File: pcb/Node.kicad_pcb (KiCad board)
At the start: 4 copper layers, 50 x 50 mm, 138 parts, among them J1 LCD, J10 SPI, J13 Power, J14 SERIAL, J2 USB_C_USB2.0_16P, J3 INDICATOR, J4 GPB[0..3], J5 GPB[4..7], J7 GPA[4..7], J8 QWIIC1, J9 QWIIC2, Q1 MMBT2222A, SW1 RESET, SW2 BOOT, U1 ESP32-S3-WROOM-1-N8R2, U2 LM66200DRLR, U3 USBLC6-2P6, U4 MCP23017_ML, U5 LD1117S33TR_SOT223

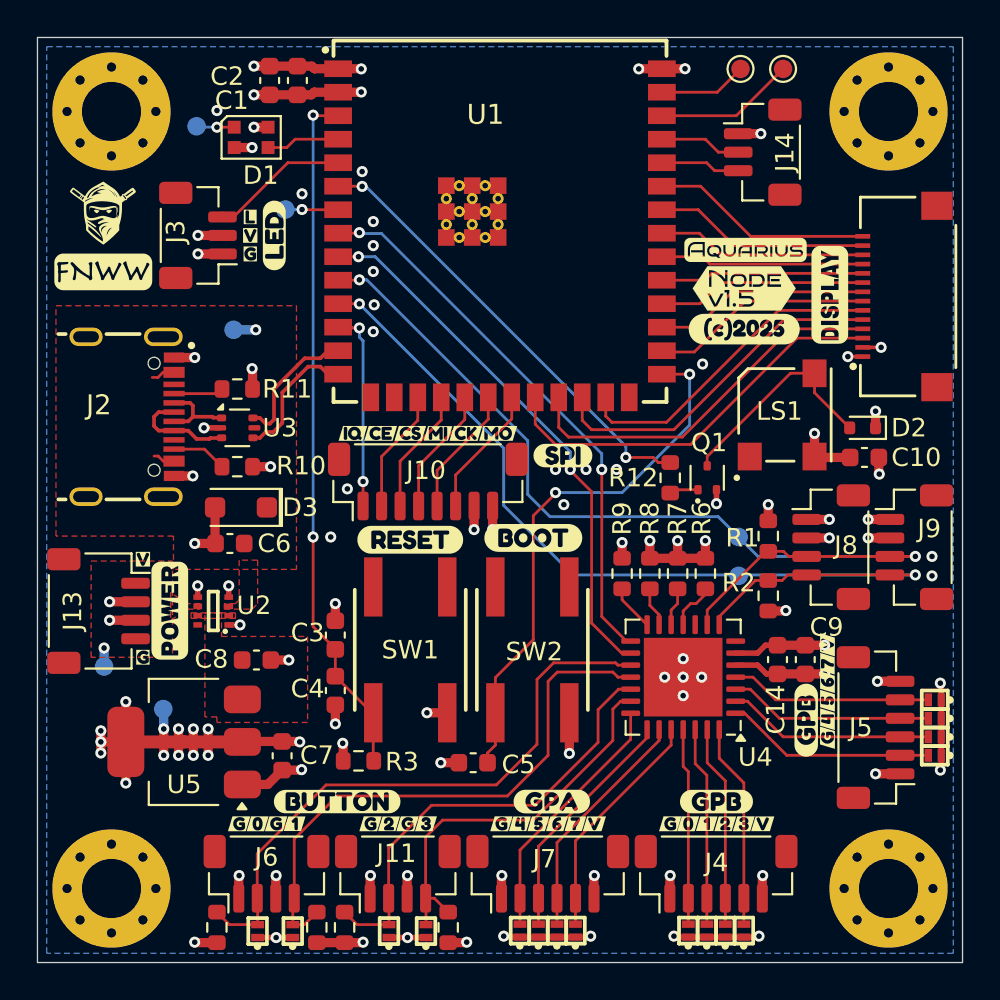
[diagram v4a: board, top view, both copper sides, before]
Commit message: Change panel to be 1x1
Changed connectors be vertical rather than horizontal.
Updated TVS diodes to DFN1006 rather than SMF
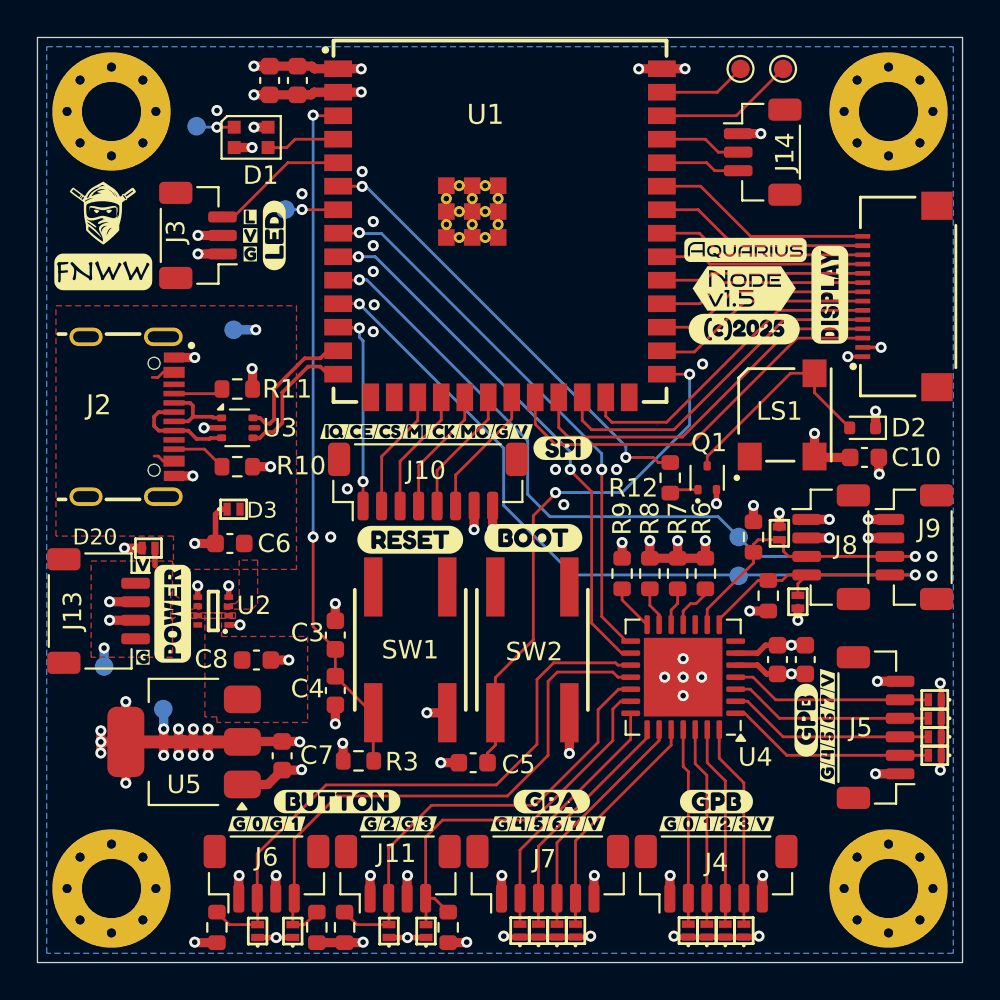
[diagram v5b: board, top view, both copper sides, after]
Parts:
- added D20: PESD5V5C1BL, CRGM Passive:DFN1006-2, F.Cu at (66.0, 77.6)
- added D21: PESD3V3S1BL, CRGM Passive:DFN1006-2, F.Cu at (101.1, 80.5)
- added D22: PESD3V3S1BL, CRGM Passive:DFN1006-2, F.Cu at (100.1, 76.8)
- added kibuzzard-68194F3F: G***, kibuzzard-68194F3F, F.Cu at (85.1, 71.3)
- added kibuzzard-68194F50: G***, kibuzzard-68194F50, F.Cu at (86.2, 71.3)
- D3: value SMF6V5A -> PESD5V5C1BL; footprint CRGM Passive:D_SOD-123F -> CRGM Passive:DFN1006-2
- moved kibuzzard-6810346D 5.68 mm to (71.3, 59.3)
- moved kibuzzard-68142030 1.93 mm to (102.7, 85.8)
- moved kibuzzard-68142039 1.93 mm to (102.7, 86.8)
- moved kibuzzard-68142043 1.93 mm to (102.7, 87.8)
- moved kibuzzard-6814204F 1.93 mm to (102.7, 88.8)
- moved kibuzzard-6815408B 1.93 mm to (102.7, 89.8)
- moved kibuzzard-68154095 1.92 mm to (102.7, 84.8)
- moved kibuzzard-6812E3C5 1.25 mm to (83.7, 71.3)
- moved kibuzzard-6812E3BB 1.20 mm to (82.0, 71.3)
- moved kibuzzard-6812E3AD 1.15 mm to (80.5, 71.3)
- moved kibuzzard-6812E3A0 1.10 mm to (79.0, 71.3)
- moved kibuzzard-6812E37E 1.05 mm to (77.5, 71.3)
- moved kibuzzard-6812E420 1.00 mm to (76.0, 71.3)
- moved R1 0.80 mm to (98.7, 77.0)
- moved kibuzzard-681035B7 0.63 mm to (69.3, 86.3)
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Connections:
- D3 pad 1: USB_5V -> GND
- D3 pad 2: GND -> USB_5V
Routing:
- net GND: track 83.6 -> 86.0 mm, vias 72 -> 75
- net I2C_SDA: track 52.6 -> 53.9 mm
- net I2C_SCL: track 51.1 -> 52.3 mm
- net LINE_5V: track 1.00 -> 1.95 mm

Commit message: Major overhaul of IO
Added GPIO module
Added SPI interface
Added serial interface
Added power selection
Added power LEDs
Changed v3.3 LDO
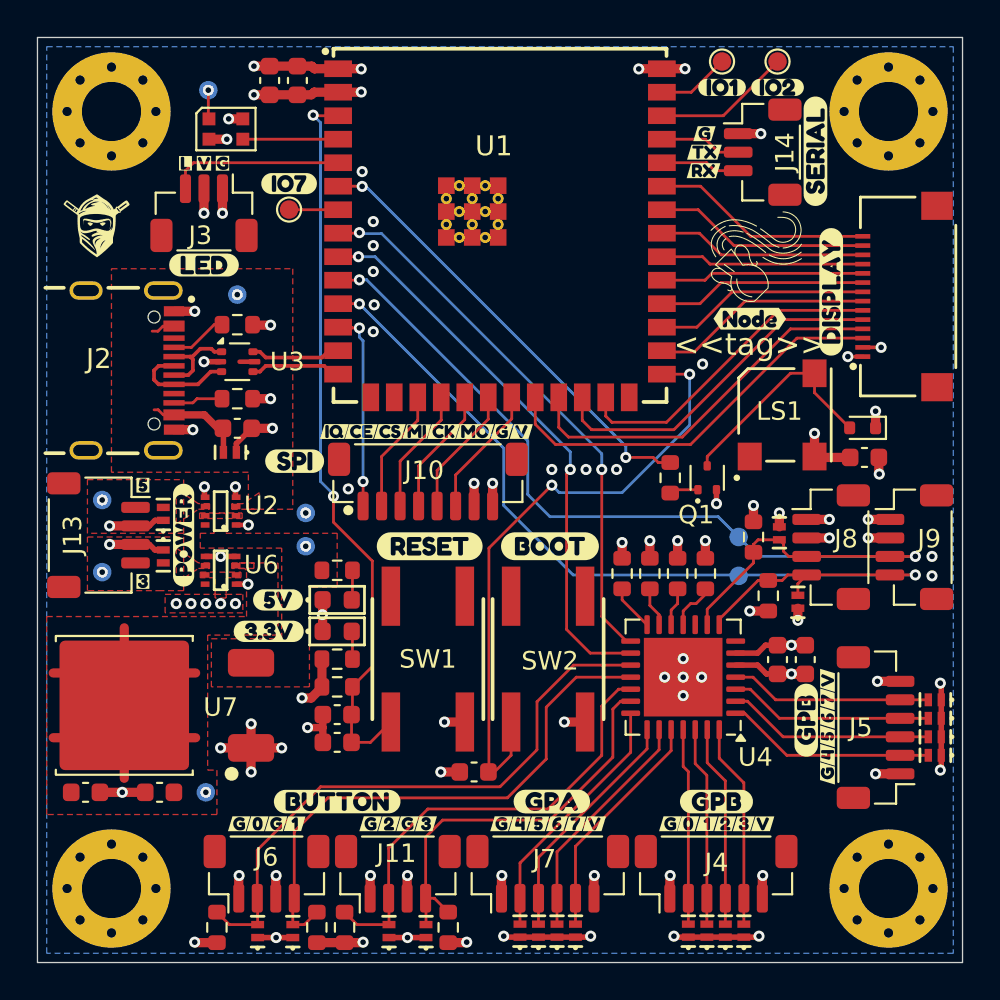
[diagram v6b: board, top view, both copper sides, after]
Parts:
- removed C7: 10uF, Capacitor_SMD:C_0603_1608Metric
- removed C8: 0.1uF, Capacitor_SMD:C_0603_1608Metric
- removed U5: LD1117S33TR_SOT223, Package_TO_SOT_SMD:SOT-223-3_TabPin2
- removed kibuzzard-67B9FE41: G***, kibuzzard-67B9FE41
- removed kibuzzard-680D0826: G***, kibuzzard-680D0826
- removed kibuzzard-68103456: G***, kibuzzard-68103456
- removed kibuzzard-681034B6: G***, kibuzzard-681034B6
- removed kibuzzard-68103896: G***, kibuzzard-68103896
- removed kibuzzard-6814216F: G***, kibuzzard-6814216F
- removed kibuzzard-6814217B: G***, kibuzzard-6814217B
- added C11: 10uF, Capacitor_SMD:C_0603_1608Metric, F.Cu at (66.6, 90.8)
- added C12: 10uF, Capacitor_SMD:C_0603_1608Metric, F.Cu at (62.6, 90.8)
- added D23: Orange, CRGM Passive:LED_0603_1608Metric, F.Cu at (76.2, 80.4)
- added D24: Blue, CRGM Passive:LED_0603_1608Metric, F.Cu at (76.2, 82.1)
- added D25: PESD3V3S1BL, CRGM Passive:DFN1006-2, F.Cu at (66.8, 78.0)
- added LOGO4: ~, CRGM Logos:Aquarius Logo 5mm, F.Cu at (101.6, 61.9)
- added R15: 4.7k, Resistor_SMD:R_0603_1608Metric, F.Cu at (76.2, 78.8)
- added R16: 1k, Resistor_SMD:R_0603_1608Metric, F.Cu at (76.2, 83.6)
- added TP11: LV33, CRGM Mechanical:TestPoint_Pad_D1.0mm, B.Cu at (63.5, 78.9)
- added TP12: V5, TestPoint:TestPoint_Pad_D1.0mm, B.Cu at (74.5, 77.5)
- added TP9: LDO_V33, TestPoint:TestPoint_Pad_D1.0mm, B.Cu at (69.1, 90.8)
- added U6: LM66200DRLR, CRGM Power:SOTFL50P160X60-8N, F.Cu at (69.9, 78.8)
- added U7: AZ1084-3.3, CRGM Power:TO-252-2, F.Cu at (64.7, 86.1)
- added kibuzzard-68194F3F: G***, kibuzzard-68194F3F, F.Cu at (96.0, 55.2)
- added kibuzzard-68366CAF: G***, kibuzzard-68366CAF, B.Cu at (69.2, 51.5)
- added kibuzzard-683921A3: G***, kibuzzard-683921A3, F.Cu at (96.0, 56.2)
- added kibuzzard-683921A8: G***, kibuzzard-683921A8, F.Cu at (96.0, 57.2)
- added kibuzzard-683921F2: G***, kibuzzard-683921F2, F.Cu at (102.0, 56.1)
- added kibuzzard-68392226: G***, kibuzzard-68392226, F.Cu at (102.9, 63.8)
- added kibuzzard-683B5370: G***, kibuzzard-683B5370, F.Cu at (65.7, 74.2)
- added kibuzzard-683B5376: G***, kibuzzard-683B5376, F.Cu at (65.7, 79.4)
- added kibuzzard-683B54B0: G***, kibuzzard-683B54B0, B.Cu at (69.1, 92.3)
- added kibuzzard-683B54F2: G***, kibuzzard-683B54F2, B.Cu at (66.0, 75.0)
- added kibuzzard-683B54FF: G***, kibuzzard-683B54FF, B.Cu at (66.4, 78.9)
- added kibuzzard-683B5656: G***, kibuzzard-683B5656, B.Cu at (76.9, 77.6)
- added kibuzzard-683B594D: G***, kibuzzard-683B594D, F.Cu at (67.9, 76.9)
- added kibuzzard-683B5CE2: G***, kibuzzard-683B5CE2, F.Cu at (73.0, 80.4)
- added kibuzzard-683B5CED: G***, kibuzzard-683B5CED, F.Cu at (72.5, 82.1)
- added kibuzzard-683C4F07: G***, kibuzzard-683C4F07, F.Cu at (98.5, 65.2)
- added kibuzzard-683C500B: G***, kibuzzard-683C500B, F.Cu at (97.0, 52.7)
- added kibuzzard-683C5017: G***, kibuzzard-683C5017, F.Cu at (100.0, 52.7)
- J10: footprint Connector_JST:JST_SH_BM08B-SRSS-TB_1x08-1MP_P1.00mm_Vertical -> CRGM Connector:JST_SH_BM08B-SRSS-TB_1x08-1MP_P1.00mm_Vertical
- J11: value ~ -> GPA[0..3]
- J13: value Power -> Power In
- J6: value ~ -> BTN[0..3]
- TP10: value VLINE -> LV5
- TP5, TP6: footprint TestPoint:TestPoint_Pad_D1.0mm -> CRGM Mechanical:TestPoint_Pad_D1.0mm
- TP7, kibuzzard-6810346D: moved to F.Cu
- TP8: footprint CRGM Mechanical:TestPoint_Pad_D1.0mm -> TestPoint:TestPoint_Pad_D1.0mm
- moved LOGO3 38.2 mm to (99.6, 65.9)
- moved kibuzzard-680D01D7 14.5 mm to (73.9, 72.9)
- moved kibuzzard-681035B7 13.4 mm to (77.5, 75.7)
- moved TP8 13.1 mm to (74.5, 75.7), turned to 180 degrees
- moved TP10 9.00 mm to (63.5, 75.0)
- moved C6 6.24 mm to (70.8, 71.1), turned to 0 degrees
- moved U2 5.41 mm to (69.9, 75.6)
- moved kibuzzard-681421A9 5.12 mm to (70.0, 56.8)
- moved kibuzzard-681421A1 4.63 mm to (69.0, 56.8)
- moved kibuzzard-68142199 4.55 mm to (68.0, 56.8)
- moved C3 4.30 mm to (76.2, 86.6), turned to 180 degrees
- moved R3 4.16 mm to (76.2, 85.1)
- moved kibuzzard-680D0262 4.12 mm to (69.0, 62.3), turned to 0 degrees
- moved J13 4.10 mm to (63.3, 76.9)
- moved R10 3.67 mm to (70.8, 69.5)
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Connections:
- J13 pad 4: unconnected-(J13-Pad4) -> LINE_V33
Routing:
- net +3.3V: track 56.6 -> 35.3 mm, vias 35 -> 27
- net LDO_V33: track 0.00 -> 16.5 mm, vias 0 -> 1
- net GND: track 86.0 -> 91.3 mm
- net BOOT: track 29.2 -> 33.7 mm
- net USB_5V: track 3.69 -> 7.54 mm
- net D_N: track 7.33 -> 4.88 mm
- net D_P: track 7.33 -> 4.92 mm
- net LINE_5V: track 1.95 -> 0.00 mm
- net LEDS: track 7.69 -> 9.40 mm
- net EN: track 38.0 -> 39.6 mm
- net /Power/V5LED: track 0.00 -> 1.62 mm
- net /Power/V3.3LED: track 0.00 -> 1.52 mm
- net OBL: track 3.97 -> 5.15 mm
- net PIO_INTB: track 29.4 -> 30.6 mm
- net Net-(U1-IO1): track 4.77 -> 3.94 mm
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- added copper zone on F.Cu, net +3.3V
- added copper zone on F.Cu, net LDO_V33
- added copper zone on F.Cu, net LINE_V33
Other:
- board text added: "<<hash>>"
- board text added: "<<tag>>"
